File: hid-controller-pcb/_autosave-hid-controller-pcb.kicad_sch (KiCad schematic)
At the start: 64 parts, among them IC1 RT9080-33GJ5, J1 10118194-0011LF, J2 Jumper, U1 STM32F103C8Tx, U3 COM-09032, U4 COM-09032, Y1 8MHz, Y2 32.768KHz

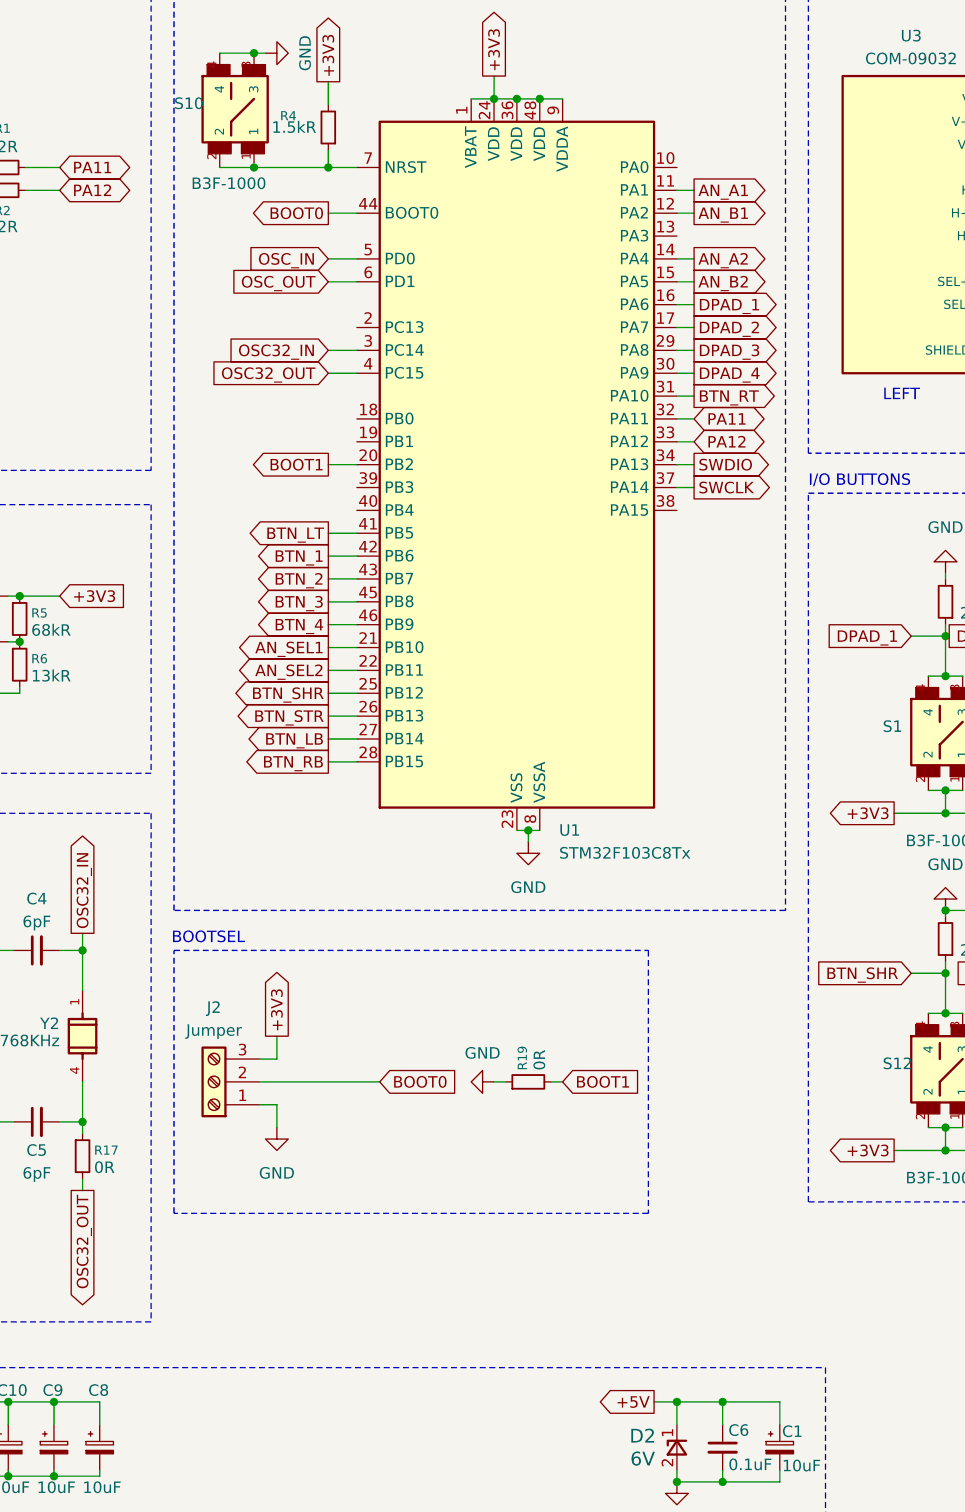
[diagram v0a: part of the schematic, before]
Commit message: working with xbox360ce remapping as a workaround for now, more work on the pcb
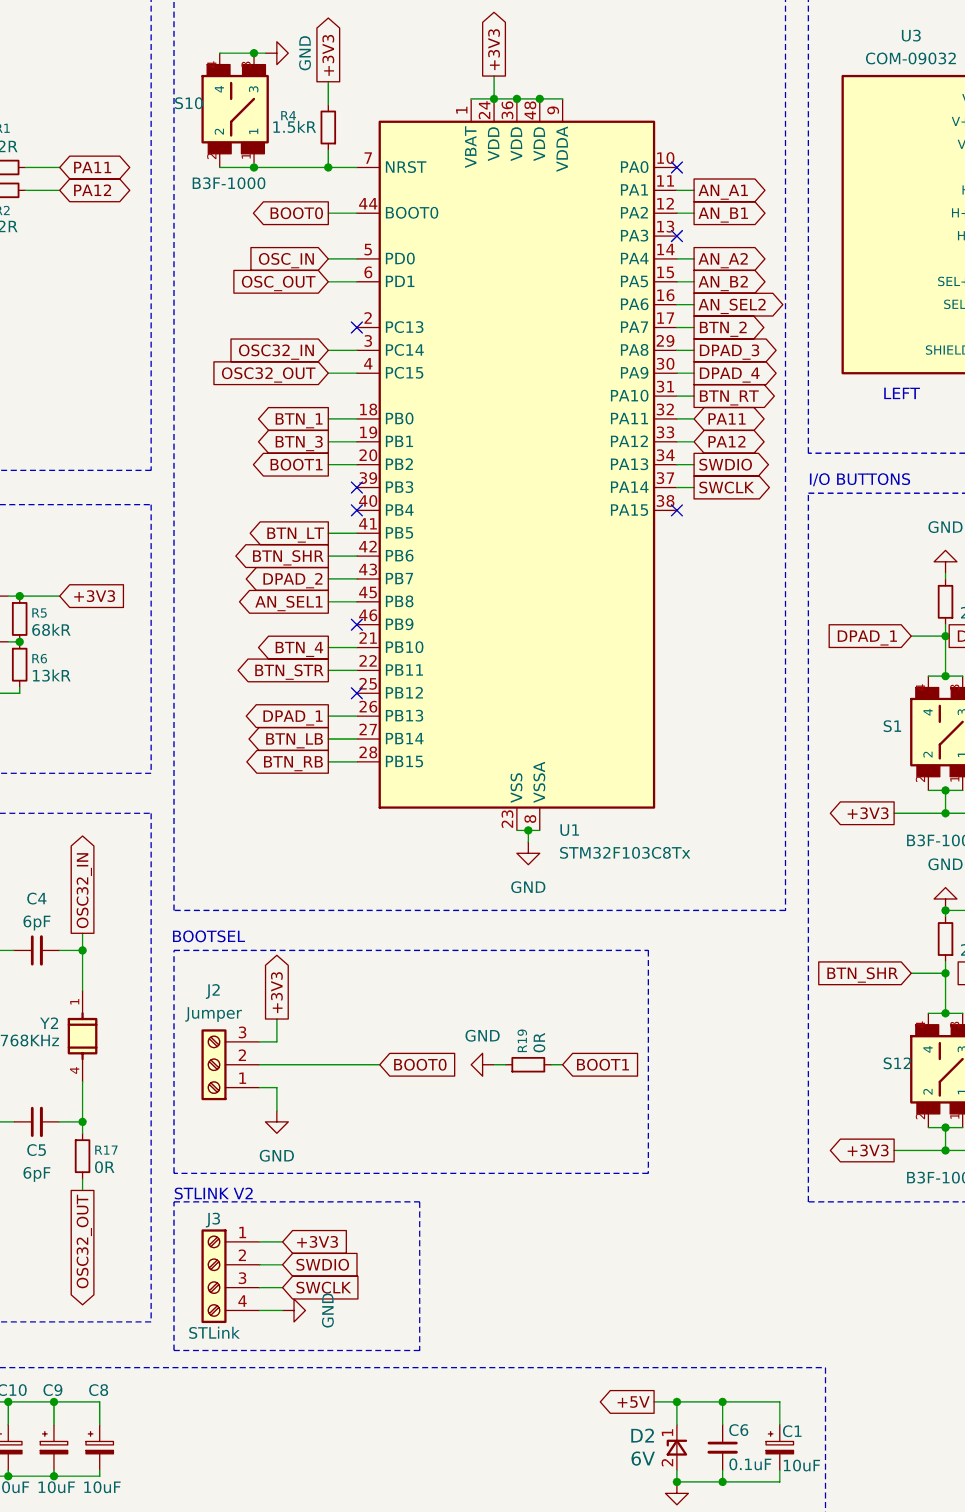
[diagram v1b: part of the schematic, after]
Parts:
- added J3: STLink, Connector_PinHeader_2.54mm:PinHeader_1x04_P2.54mm_Vertical, symbol Connector:Screw_Terminal_01x04
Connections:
- net +3V3: now also J3.1 (Pin_1)
- net AN_SEL1: now also U1.45 (PB8); no longer U1.21 (PB10)
- net AN_SEL2: now also U1.16 (PA6); no longer U1.22 (PB11)
- net BTN_1: now also U1.18 (PB0); no longer U1.42 (PB6)
- net BTN_2: now also U1.17 (PA7); no longer U1.43 (PB7)
- net BTN_3: now also U1.19 (PB1); no longer U1.45 (PB8)
- net BTN_4: now also U1.21 (PB10); no longer U1.46 (PB9)
- net BTN_SHR: now also U1.42 (PB6); no longer U1.25 (PB12)
- net BTN_STR: now also U1.22 (PB11); no longer U1.26 (PB13)
- net DPAD_1: now also U1.26 (PB13); no longer U1.16 (PA6)
- net DPAD_2: now also U1.43 (PB7); no longer U1.17 (PA7)
- net GND: now also J3.4 (Pin_4)
- net SWCLK: now also J3.3 (Pin_3)
- net SWDIO: now also J3.2 (Pin_2)
- no-connect marks 0 -> 8
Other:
- note added: "STLINK V2"
- moved on the sheet: J2, R19

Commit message: switched to 4 layer board, too many traces :(
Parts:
- C8, C9: value 10uF -> 1uF; footprint lib:CAPAE530X550N -> Capacitor_SMD:C_0603_1608Metric
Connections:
- net +3V3: now also R3.1
- net +5V: no longer R3.1
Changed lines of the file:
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@@
 	)
 	(junction
+		(at 48.26 38.735)
+		(diameter 0)
+		(color 0 0 0 0)
+	)
+	(junction
 		(at 162.56 105.41)
 		(diameter 0)
@@
 	)
 	(junction
-		(at 48.26 38.735)
-		(diameter 0)
-		(color 0 0 0 0)
-	)
-	(junction
 		(at 46.99 181.61)
 		(diameter 0)
@@
 	(wire
 		(pts
-			(xy 41.275 38.735) (xy 48.26 38.735)
-		)
-		(stroke
-			(width 0)
-			(type default)
-		)
-	)
-	(wire
-		(pts
 			(xy 44.45 94.615) (xy 44.45 96.52)
 		)
@@
 	(wire
 		(pts
+			(xy 41.275 38.735) (xy 48.26 38.735)
+		)
+		(stroke
+			(width 0)
+			(type default)
+		)
+	)
+	(wire
+		(pts
 			(xy 224.79 125.095) (xy 224.79 129.54)
 		)
@@
 		)
 	)
-	(global_label "+5V"
-		(shape input)
-		(at 48.26 48.895 270)
-		(fields_autoplaced yes)
-		(effects
-			(font
-				(size 1.27 1.27)
-			)
-			(justify right)
-		)
-		(property "Intersheetrefs" "${INTERSHEET_REFS}"
-			(at 48.26 55.7507 90)
-			(hide yes)
-			(show_name no)
-			(do_not_autoplace no)
-			(effects
-				(font
-					(size 1.27 1.27)
-				)
-				(justify right)
-			)
-		)
-	)
 	(global_label "OSC32_OUT"
 		(shape input)
@@
 	(global_label "+3V3"
 		(shape output)
+		(at 48.26 48.895 270)
+		(fields_autoplaced yes)
+		(effects
+			(font
+				(size 1.27 1.27)
+			)
+			(justify right)
+		)
+		(property "Intersheetrefs" "${INTERSHEET_REFS}"
+			(at 48.26 55.921 90)
+			(hide yes)
+			(show_name no)
+			(do_not_autoplace no)
+			(effects
+				(font
+					(size 1.27 1.27)
+				)
+				(justify right)
+			)
+		)
+	)
+	(global_label "+3V3"
+		(shape output)
 		(at 219.075 107.95 180)
 		(fields_autoplaced yes)
@@
 			)
 		)
-		(property "Value" "10uF"
+		(property "Value" "1uF"
 			(at 61.595 182.88 0)
 			(show_name no)
@@
 			)
 		)
-		(property "Footprint" "lib:CAPAE530X550N"
+		(property "Footprint" "Capacitor_SMD:C_0603_1608Metric"
 			(at 63.5 178.435 0)
 			(hide yes)
@@
 			)
 		)
-		(property "Value" "10uF"
+		(property "Value" "1uF"
 			(at 66.675 182.88 0)
 			(show_name no)
@@
 			)
 		)
-		(property "Footprint" "lib:CAPAE530X550N"
+		(property "Footprint" "Capacitor_SMD:C_0603_1608Metric"
 			(at 68.58 178.435 0)
 			(hide yes)

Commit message: further work on controller
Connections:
- net BTN_RT: now also U1.26 (PB13); no longer U1.31 (PA10)
- net DPAD_1: now also U1.31 (PA10); no longer U1.26 (PB13)
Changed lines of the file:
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@@
 	(global_label "DPAD_1"
 		(shape output)
-		(at 93.98 97.155 180)
-		(fields_autoplaced yes)
-		(effects
-			(font
-				(size 1.27 1.27)
-			)
-			(justify right)
-		)
-		(property "Intersheetrefs" "${INTERSHEET_REFS}"
-			(at 84.8224 97.155 0)
-			(hide yes)
-			(show_name no)
-			(do_not_autoplace no)
-			(effects
-				(font
-					(size 1.27 1.27)
-				)
-				(justify right)
+		(at 134.62 61.595 0)
+		(fields_autoplaced yes)
+		(effects
+			(font
+				(size 1.27 1.27)
+			)
+			(justify left)
+		)
+		(property "Intersheetrefs" "${INTERSHEET_REFS}"
+			(at 143.7776 61.595 0)
+			(hide yes)
+			(show_name no)
+			(do_not_autoplace no)
+			(effects
+				(font
+					(size 1.27 1.27)
+				)
+				(justify left)
 			)
 		)
@@
 	(global_label "BTN_RT"
 		(shape output)
-		(at 134.62 61.595 0)
-		(fields_autoplaced yes)
-		(effects
-			(font
-				(size 1.27 1.27)
-			)
-			(justify left)
-		)
-		(property "Intersheetrefs" "${INTERSHEET_REFS}"
-			(at 143.7776 61.595 0)
-			(hide yes)
-			(show_name no)
-			(do_not_autoplace no)
-			(effects
-				(font
-					(size 1.27 1.27)
-				)
-				(justify left)
-			)
-		)
+		(at 93.98 97.155 180)
+		(fields_autoplaced yes)
+		(effects
+			(font
+				(size 1.27 1.27)
+			)
+			(justify right)
+		)
+		(property "Intersheetrefs" "${INTERSHEET_REFS}"
+			(at 84.8224 97.155 0)
+			(hide yes)
+			(show_name no)
+			(do_not_autoplace no)
+			(effects
+				(font
+					(size 1.27 1.27)
+				)
+				(justify right)
+			)
+		)

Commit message: Controller layout done! Reviewing before sending to JLC
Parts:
- C11, C9: now not fitted
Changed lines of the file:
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@@
 		(exclude_from_sim no)
 		(in_bom yes)
-		(on_board yes)
+		(on_board no)
 		(in_pos_files yes)
-		(dnp no)
+		(dnp yes)
 		(property "Reference" "C9"
 			(at 62.23 172.085 0)
@@
 		(exclude_from_sim no)
 		(in_bom yes)
-		(on_board yes)
+		(on_board no)
 		(in_pos_files yes)
-		(dnp no)
+		(dnp yes)
 		(property "Reference" "C11"
 			(at 52.07 172.085 0)
